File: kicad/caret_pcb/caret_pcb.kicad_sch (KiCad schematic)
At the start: 0 parts

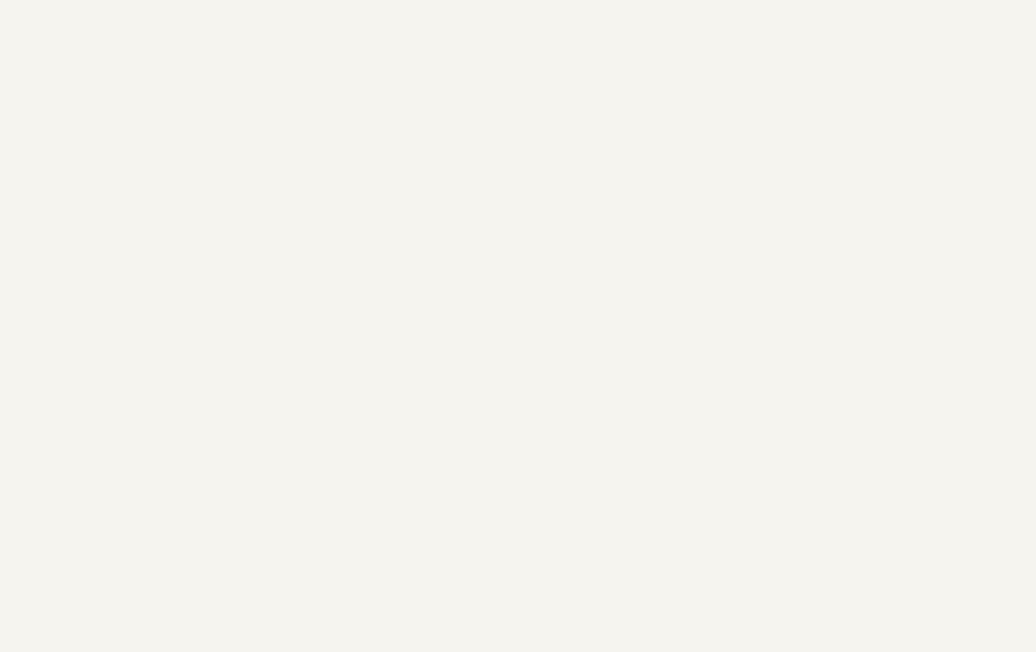
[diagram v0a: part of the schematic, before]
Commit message: kicad.caret_pcb: add 3d printer boards
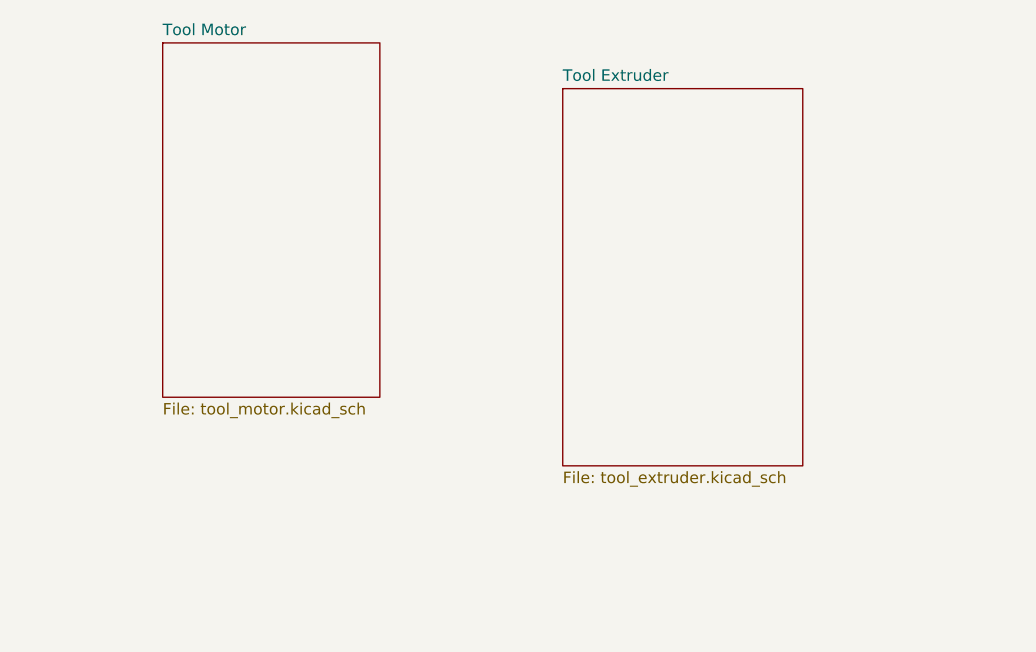
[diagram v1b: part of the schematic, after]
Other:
- added sheet Tool Extruder (tool_extruder.kicad_sch)
- added sheet Tool Motor (tool_motor.kicad_sch)
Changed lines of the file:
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@@
+    )
+  )
+  (sheet (at 109.22 38.1) (size 24.13 39.37) (fields_autoplaced)
+    (stroke (width 0.1524) (type solid) (color 0 0 0 0))
+    (fill (color 0 0 0 0.0000))
+    (property "Sheet name" "Tool Motor" (id 0) (at 109.22 37.3884 0)
+      (effects (font (size 1.27 1.27)) (justify left bottom))
+    )
+    (property "Sheet file" "tool_motor.kicad_sch" (id 1) (at 109.22 78.0546 0)
+      (effects (font (size 1.27 1.27)) (justify left top))
     )
   )
@@
     (pin "+5V" input (at 99.06 172.72 180)
       (effects (font (size 1.27 1.27)) (justify left))
+    )
+  )
+  (sheet (at 153.67 43.18) (size 26.67 41.91) (fields_autoplaced)
+    (stroke (width 0.1524) (type solid) (color 0 0 0 0))
+    (fill (color 0 0 0 0.0000))
+    (property "Sheet name" "Tool Extruder" (id 0) (at 153.67 42.4684 0)
+      (effects (font (size 1.27 1.27)) (justify left bottom))
+    )
+    (property "Sheet file" "tool_extruder.kicad_sch" (id 1) (at 153.67 85.6746 0)
+      (effects (font (size 1.27 1.27)) (justify left top))
     )
   )
@@
     (path "/0243fc01-c89d-427f-ada0-c7b78b375c4b" (page "4"))
     (path "/78e2c7a0-0fe9-440e-ab14-9611b86fc8cb" (page "5"))
+    (path "/35119bf0-23c9-4bb2-becd-2a858b5cb4d5" (page "6"))
+    (path "/88560847-ae10-4705-b2a9-799bbf32e0fc" (page "7"))
   )
   (symbol_instances
@@
       (reference "D5") (unit 1) (value "BLUE") (footprint "Diode_SMD:D_0805_2012Metric")
     )
+    (path "/88560847-ae10-4705-b2a9-799bbf32e0fc/ad9cd185-93cd-4d1a-bc79-eb3cd44db75b"
+      (reference "D?") (unit 1) (value "LED_Filled") (footprint "LED_SMD:LED_PLCC_2835")
+    )
     (path "/0674c5a1-ca4b-4b6b-aa60-3847e1a37d52/9b2243e1-b4a5-4d8d-b925-203eb710e075"
       (reference "J1") (unit 1) (value "RAMPS POWER IN") (footprint "Connector_JST:JST_XH_B4B-XH-A_1x04_P2.50mm_Vertical")
@@
       (reference "J15") (unit 1) (value "PWR IN") (footprint "Connector_JST:JST_XH_B2B-XH-A_1x02_P2.50mm_Vertical")
     )
+    (path "/88560847-ae10-4705-b2a9-799bbf32e0fc/00672a55-4382-40ef-af60-f37336738671"
+      (reference "J?") (unit 1) (value "T.ext") (footprint "")
+    )
+    (path "/88560847-ae10-4705-b2a9-799bbf32e0fc/077384ec-a581-49ad-af44-ec7b3a27e958"
+      (reference "J?") (unit 1) (value "T.hbr") (footprint "")
+    )
+    (path "/88560847-ae10-4705-b2a9-799bbf32e0fc/0f9db253-2dc4-425a-8711-82a5b930da1b"
+      (reference "J?") (unit 1) (value "Stepper") (footprint "")
+    )
+    (path "/88560847-ae10-4705-b2a9-799bbf32e0fc/82a136d8-6c7b-4689-bb30-d476f4678c1a"
+      (reference "J?") (unit 1) (value "TOOLHEAD") (footprint "Connector_JST:JST_XH_B12B-XH-A_1x12_P2.50mm_Vertical")
+    )
+    (path "/88560847-ae10-4705-b2a9-799bbf32e0fc/b17ae402-ae49-4ceb-bf50-99a7d1dce2e2"
+      (reference "J?") (unit 1) (value "PWR IN") (footprint "Connector_JST:JST_XH_B4B-XH-A_1x04_P2.50mm_Vertical")
+    )
+    (path "/35119bf0-23c9-4bb2-becd-2a858b5cb4d5/f26c481d-d67e-4482-a7d9-6f79748d485a"
+      (reference "J?") (unit 1) (value "Conn_01x02_Male") (footprint "")
+    )
+    (path "/88560847-ae10-4705-b2a9-799bbf32e0fc/4d8ffbb9-4b7c-4337-81da-35463caa6407"
+      (reference "LS?") (unit 1) (value "7BB-12-9") (footprint "Speak_Murata_7BB:Murata-7BB-12-9-MFG")
+    )
+    (path "/88560847-ae10-4705-b2a9-799bbf32e0fc/7a7ccb21-53b7-43cb-b537-0b377a1cd2f1"
+      (reference "LS?") (unit 1) (value "7BB-12-9") (footprint "Speak_Murata_7BB:Murata-7BB-12-9-MFG")
+    )
     (path "/78e2c7a0-0fe9-440e-ab14-9611b86fc8cb/707c1dbd-ad7b-48a0-8f2e-9fa5c9b5d1f6"
       (reference "POT1") (unit 1) (value "TC33X-2-105") (footprint "digikey-footprints:Trimpot_3.8mmx3.6mm_TC33X-2-103E")
@@
       (reference "U2") (unit 4) (value "LM324") (footprint "Package_SO:SOIC-14_3.9x8.7mm_P1.27mm")
     )
-  )
+    (path "/35119bf0-23c9-4bb2-becd-2a858b5cb4d5/80f86dbb-173a-407f-b1a5-5b28f6434658"
+      (reference "U?") (unit 1) (value "A4950E") (footprint "Package_SO:SOIC-8-1EP_3.9x4.9mm_P1.27mm_EP2.41x3.3mm")
+    )
+  )
